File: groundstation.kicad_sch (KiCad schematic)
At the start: 0 parts

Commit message: added display receptacle port for 7in TFT
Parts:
- added C1: C_Small_US, Capacitor_THT:C_Disc_D3.0mm_W1.6mm_P2.50mm, symbol Device:C_Small_US
- added J1: USB_C_Receptacle_USB2.0_16P, Connector_USB:USB_C_Receptacle_G-Switch_GT-USB-7010ASV, symbol Connector:USB_C_Receptacle_USB2.0_16P
- added J2: 62684-402100ALF, CONN_62684-402100ALF_AMP, symbol FCC 40 0.5mm:62684-402100ALF
- added R1, R2: 22, Resistor_SMD:R_0402_1005Metric, symbol Device:R_Small
- added R3, R4: 5.1k, Resistor_SMD:R_0402_1005Metric, symbol Device:R_Small
- added R5: R_Small, Capacitor_THT:C_Disc_D3.0mm_W1.6mm_P2.50mm, symbol Device:R_Small
- added SW1: SW_Push, Resistor_SMD:R_0402_1005Metric, symbol Switch:SW_Push
- added U1: ESP32-S3-WROOM-1, RF_Module:ESP32-S3-WROOM-1, symbol RF_Module:ESP32-S3-WROOM-1
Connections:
- new net: C1.1, R5.1, SW1.2
- new net: J1.B5 (CC2), R4.2
- new net: R1.1, U1.13 (USB_D-)
- new net: R2.1, U1.14 (USB_D+)
- new net: R5.2, U1.3 (EN)
- new net: J1.A6 (D+), J1.B6 (D+), R2.2
- new net: J1.A7 (D-), J1.B7 (D-), R1.2
- new net: J1.A5 (CC1), R3.2
- new net +3V3: U1.2 (3V3)
- new net GND: C1.2, J1.A1 (GND), J1.A12 (GND), J1.B1 (GND), J1.B12 (GND), J1.S1 (SHIELD), R3.1, R4.1, SW1.1, U1.1 (GND), U1.40 (GND), U1.41 (GND)
- new net VBUS: J1.A4 (VBUS), J1.A9 (VBUS), J1.B4 (VBUS), J1.B9 (VBUS)
- no-connect marks 0 -> 6

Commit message: Update schematicand PCB
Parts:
- removed C1: C_Small_US, Capacitor_THT:C_Disc_D3.0mm_W1.6mm_P2.50mm, symbol Device:C_Small_US
- removed J2: 62684-402100ALF, CONN_62684-402100ALF_AMP, symbol FCC 40 0.5mm:62684-402100ALF
- added 2.2uF1, 2.2uF2: C_Small_US, Capacitor_SMD:C_0402_1005Metric, symbol Device:C_Small_US
- added C1: ?, symbol Device:C
- added C10: 1u, symbol Device:C
- added C11: 22u, Capacitor_SMD:C_0603_1608Metric, symbol Device:C
- added C12: 10u, symbol Device:C
- added C2, C3, C4, C5, C6: 1uF, Capacitor_SMD:C_0402_1005Metric, symbol Device:C_Small_US
- added C7: 10u, symbol Device:C_Polarized
- added C8: 0.1u, symbol Device:C
- added C9: 2.2uF, Capacitor_SMD:C_0402_1005Metric, symbol Device:C_Small_US
- added DS1: NHD-C12832A1Z-FSW-FBW-3V3, Ground_Station:LCD_NHD-C12832A1Z-FSW-FBW-3V3, symbol NHD LCD display:NHD-C12832A1Z-FSW-FBW-3V3
- added LED1: LTST-C170KRKT, Ground_Station:LED_LTST-C170KRKT_LTO-M, symbol LTST-C170krkt:LTST-C170KRKT
- added R6: 410, symbol Device:R_Small
- added R7: 10k, Resistor_SMD:R_0402_1005Metric, symbol Device:R_Small
- added U3: AMS1117-3.3, Package_TO_SOT_SMD:SOT-223-3_TabPin2, symbol Regulator_Linear:AMS1117-3.3
- R5: value R_Small -> ?; footprint Capacitor_THT:C_Disc_D3.0mm_W1.6mm_P2.50mm -> Resistor_SMD:R_0402_1005Metric
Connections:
- net +3V3: now also C11.1, C7.1, C8.1, DS1.12 (VDD), DS1.A (LED+), LED1.2, R7.2, U3.2 (VO)
- net GND: now also C1.1, C10.1, C11.2, C12.2, C2.1, C3.1, C4.1, C5.1, C6.1, C7.2, C8.2, C9.1, DS1.11 (VSS), DS1.K (LED-), R6.1, U3.1 (GND)
- net at R5.1, SW1.2: now also C1.2
- net SCL: now reaches U1.15 (IO3)
- net SCL: now also DS1.14 (SCL)
- net CS1: now reaches U1.27 (IO0)
- net CS1: now also DS1.17 (~{CS1})
- net EN: now reaches R5.2, U1.3 (EN)
- net EN: now also C10.2, R7.1
- net A0: now reaches U1.38 (IO2)
- net A0: now also DS1.15 (A0)
- net RST: now reaches U1.39 (IO1)
- net RST: now also DS1.16 (~{RST})
- net SI: now reaches U1.4 (IO4)
- net SI: now also DS1.13 (SI)
- net VBUS renamed 5V
- net 5V: now also C12.1, U3.3 (VI)
- new net: LED1.1, R6.2
- new net: 2.2uF2.2, DS1.6 (C2-)
- new net: 2.2uF2.1, DS1.7 (C2+)
- new net: 2.2uF1.1, DS1.8 (C1+)
- new net: 2.2uF1.2, DS1.9 (C1-)
- new net V0: C2.2, DS1.1 (V0)
- new net V1: C3.2, DS1.2 (V1)
- new net V2: C4.2, DS1.3 (V2)
- new net V3: C5.2, DS1.4 (V3)
- new net V4: C6.2, DS1.5 (V4)
- new net Vout: C9.2, DS1.10 (VOUT)
- no-connect marks 6 -> 31
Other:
- note added: "Power LDO for Vdd"
- note added: "coupling caps for the display"
- moved on the sheet: J1, R1, R2, R3, R4, R5, SW1, U1

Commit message: done with schematic (hopefully)
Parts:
- removed 2.2uF1, 2.2uF2: C_Small_US, Capacitor_SMD:C_0402_1005Metric, symbol Device:C_Small_US
- removed C2, C3, C4, C5, C6: 1uF, Capacitor_SMD:C_0402_1005Metric, symbol Device:C_Small_US
- removed C7: 10u, symbol Device:C_Polarized
- removed C9: 2.2uF, Capacitor_SMD:C_0402_1005Metric, symbol Device:C_Small_US
- removed LED1: LTST-C170KRKT, Ground_Station:LED_LTST-C170KRKT_LTO-M, symbol LTST-C170krkt:LTST-C170KRKT
- added C13, C14: 2.2uF, Capacitor_SMD:C_0402_1005Metric, symbol Device:C
- added C2: 2.2u, Capacitor_SMD:C_0402_1005Metric, symbol Device:C
- added C3, C4, C6, C9: 1u, Capacitor_SMD:C_0402_1005Metric, symbol Device:C
- added C5: 1.0u, Capacitor_SMD:C_0402_1005Metric, symbol Device:C
- added C7: 10uF, Capacitor_SMD:C_0805_2012Metric, symbol Device:C
- added D1: LED, LED_THT:LED_D1.8mm_W1.8mm_H2.4mm_Horizontal_O1.27mm_Z1.6mm, symbol Device:LED
- added J2: Conn_01x02_Pin, Connector_PinHeader_2.54mm:PinHeader_1x02_P2.54mm_Vertical, symbol Connector:Conn_01x02_Pin
- C1: value ? -> 0.1u; footprint (none) -> Capacitor_SMD:C_0402_1005Metric
- C10: footprint (none) -> Capacitor_SMD:C_0402_1005Metric
- C11: footprint Capacitor_SMD:C_0603_1608Metric -> Capacitor_SMD:C_0805_2012Metric
- C12, C8: footprint (none) -> Capacitor_SMD:C_0805_2012Metric
- R5: value ? -> 0
- R6: footprint (none) -> Resistor_SMD:R_0402_1005Metric
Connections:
- net +3V3: now also C7.1, D1.2 (A)
- net GND: now also C2.2, C3.2, C4.2, C5.2, C6.2, C7.2, C9.2, J2.2 (Pin_2)
- net at R6.2: now also D1.1 (K)
- net Display_SI: now reaches U1.5 (IO5)
- net Display_SI: now also DS1.13 (SI)
- net at DS1.6 (C2-): now also C13.2
- net at DS1.7 (C2+): now also C13.1
- net at DS1.8 (C1+): now also C14.1
- net at DS1.9 (C1-): now also C14.2
- net A0 renamed Display_A0
- net Display_A0: now also U1.15 (IO3); no longer U1.38 (IO2)
- net CS1: no longer names the net of U1.27 (IO0)
- net CS1: now also J2.1 (Pin_1); no longer DS1.17 (~{CS1})
- net RST renamed Display_CS1
- net Display_CS1: now also DS1.17 (~{CS1}); no longer DS1.16 (~{RST})
- net SCL renamed Display_SCL
- net Display_SCL: now also U1.4 (IO4); no longer U1.15 (IO3)
- removed net SI: DS1.13 (SI), U1.4 (IO4)
- net V0: no longer names the net of DS1.1 (V0)
- net V0: now also C9.1
- net V1: no longer names the net of DS1.2 (V1)
- net V1: now also C6.1
- net V2: no longer names the net of DS1.3 (V2)
- net V2: now also C5.1
- net V3: no longer names the net of DS1.4 (V3)
- net V3: now also C4.1
- net V4: no longer names the net of DS1.5 (V4)
- net V4: now also C3.1
- net Vout: no longer names the net of DS1.10 (VOUT)
- net Vout: now also C2.1
- new net Display_RST: DS1.16 (~{RST}), U1.38 (IO2)
- no-connect marks 31 -> 30
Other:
- note added: "Charging Pumps for LCD"
- note added: "EN pull up circuit and OFF switch"
- note added: "ESP32-S3 indicator LED"
- note added: "Power LDO for usb 5V to esp32 3V3 VDD"
- note added: "low and high frequency filter"
- note removed: "Power LDO for Vdd"
- note removed: "coupling caps for the display"
- moved on the sheet: C1, C10, C11, C12, DS1, R5, R6, R7, SW1, U3

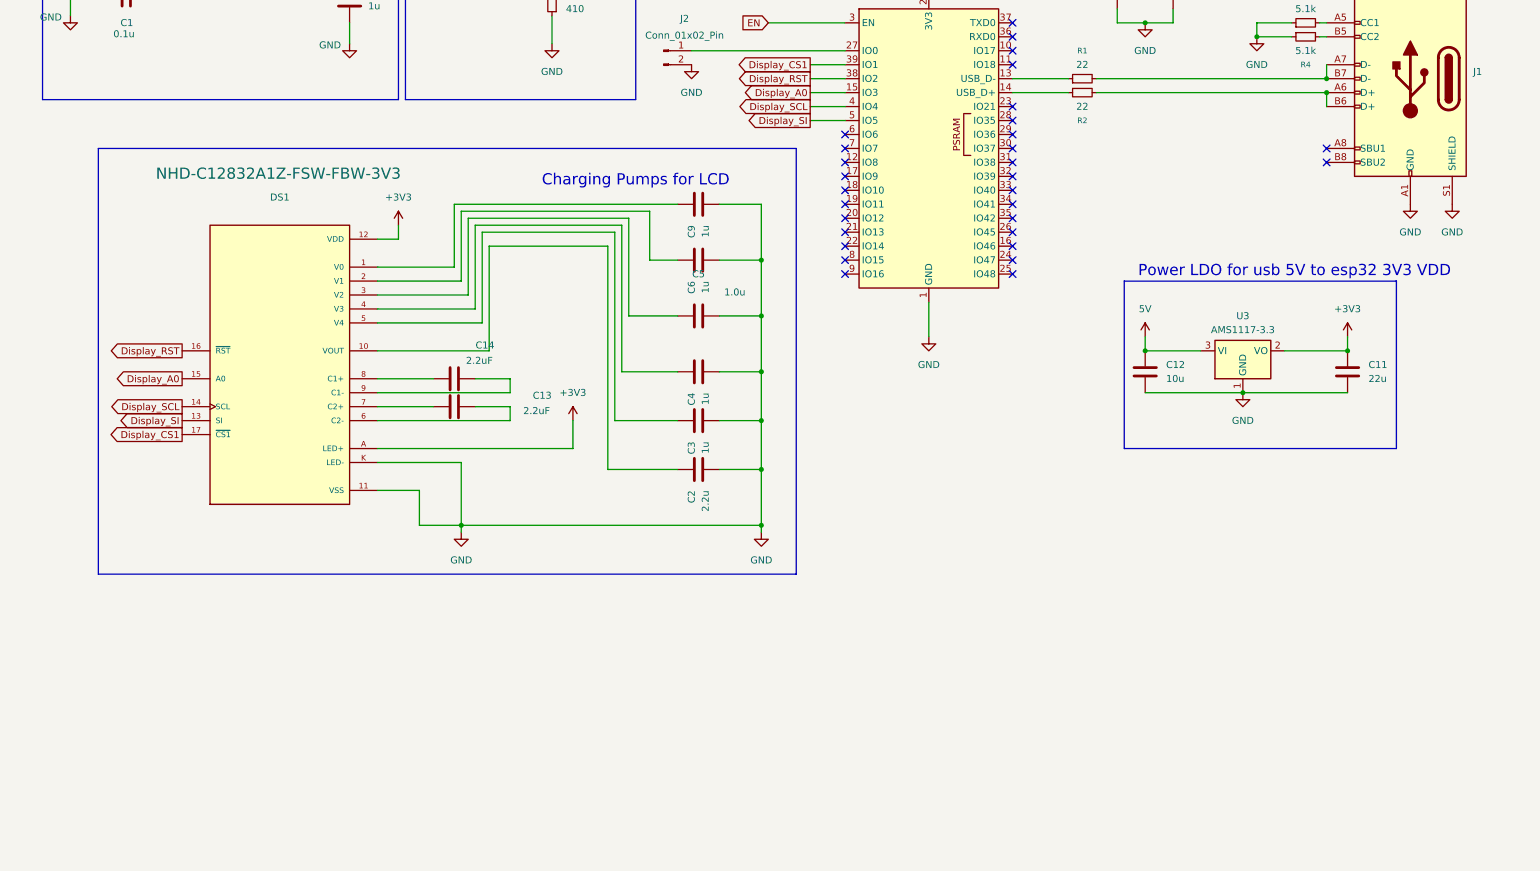
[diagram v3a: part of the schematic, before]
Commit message: added GPS module
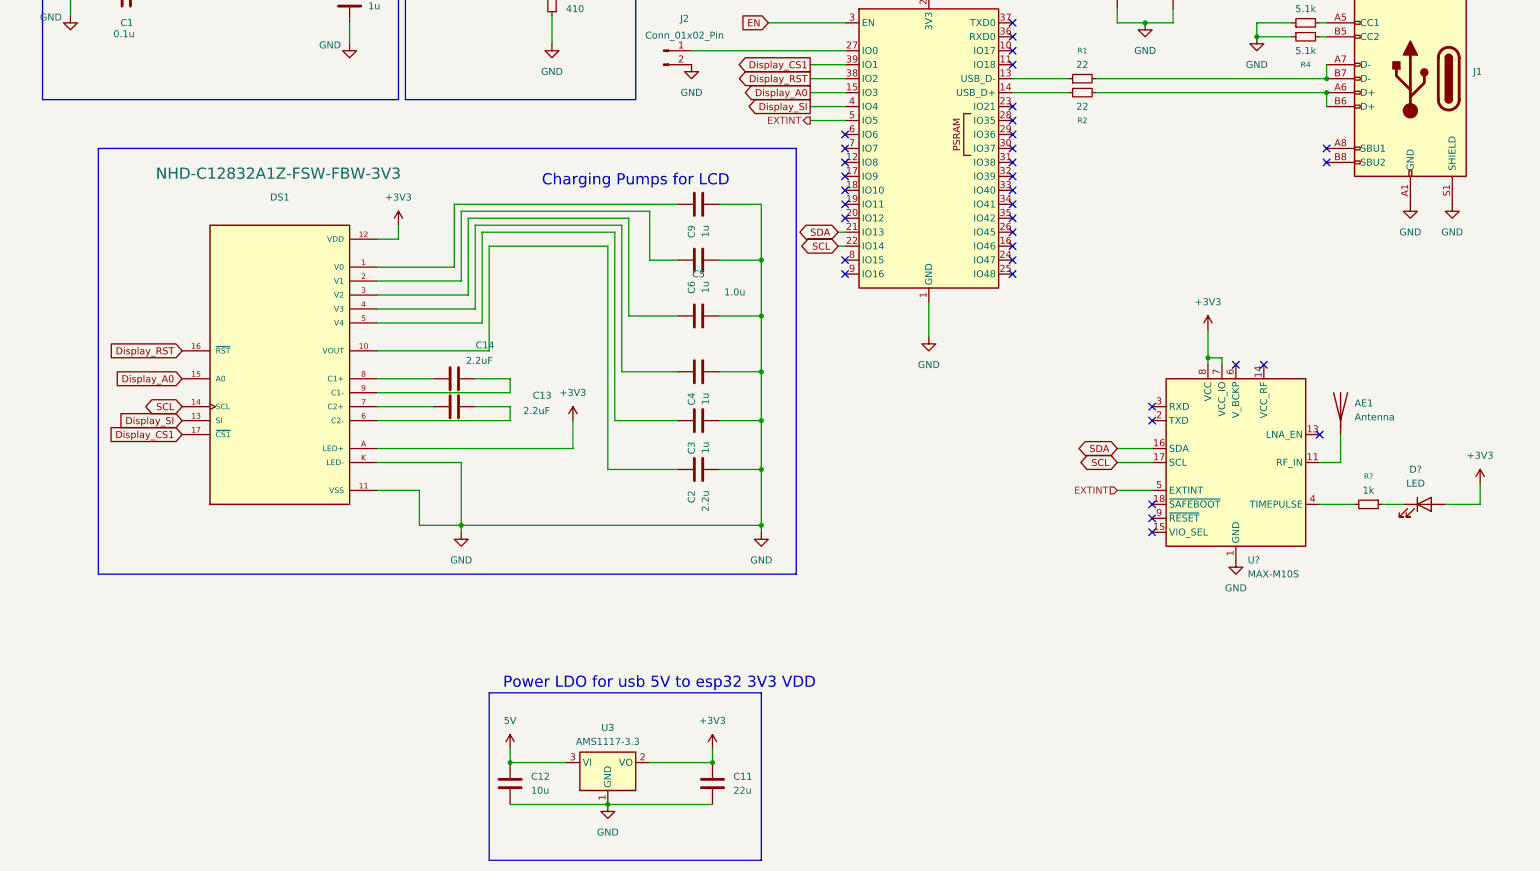
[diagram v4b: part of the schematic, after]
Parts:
- added AE1: Antenna, symbol Device:Antenna
- added D?: LED, LED_SMD:LED_0805_2012Metric, symbol Device:LED
- added R?: 1k, Resistor_SMD:R_0402_1005Metric, symbol Device:R_Small
- added U?: MAX-M10S, RF_GPS:ublox_MAX, symbol RF_GPS:MAX-M10S
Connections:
- net +3V3: now also D?.2 (A), U?.7 (VCC_IO), U?.8 (VCC)
- net Display_SI: now also U1.4 (IO4); no longer U1.5 (IO5)
- net GND: now also U?.1 (GND), U?.10 (GND), U?.12 (GND)
- net SDA: now reaches U1.21 (IO13)
- net SDA: now also U?.16 (SDA)
- net SCL: now reaches U1.22 (IO14)
- net SCL: now also DS1.14 (SCL), U?.17 (SCL)
- removed net Display_SCL: DS1.14 (SCL), U1.4 (IO4)
- new net: AE1.1 (A), U?.11 (RF_IN)
- new net: R?.2, U?.4 (TIMEPULSE)
- new net: D?.1 (K), R?.1
- new net EXTINT: U1.5 (IO5), U?.5 (EXTINT)
- no-connect marks 30 -> 36
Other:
- moved on the sheet: C11, C12, U3

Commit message: dunno, random adds
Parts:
- added C15, C16, C17, C18, C19: C_Small, symbol Device:C_Small
- added FL1: 0900FM15K0039, RF_Converter:Balun_Johanson_0900FM15K0039, symbol Filter:0900FM15K0039
- added J3: Conn_Coaxial, Connector_Coaxial:SMA_Samtec_SMA-J-P-H-ST-EM1_EdgeMount, symbol Connector:Conn_Coaxial
- added L1, L2: L_Small, symbol Device:L_Small
- added U4: SX1262IMLTRT, Package_DFN_QFN:QFN-24-1EP_4x4mm_P0.5mm_EP2.6x2.6mm, symbol RF:SX1262IMLTRT
- added U5: BGS12WN6E6327, Package_LGA:Infineon_PG-TSNP-6-10_0.7x1.1mm_0.7x1.1mm_P0.4mm, symbol RF_Switch:BGS12WN6E6327
- AE1: footprint (none) -> Connector_Coaxial:SMA_BAT_Wireless_BWSMA-KWE-Z001
- gave numbers to parts that had none: 3
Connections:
- net GND: now also C15.2, C16.2, C18.2, C19.2, J3.2 (Ext), U4.2 (GND), U4.20 (GND), U4.25 (GND), U4.5 (GND), U4.8 (GND)
- new net: C15.1, C16.1, L1.2, U4.24 (VR_PA)
- new net: C17.1, C18.1, L2.1
- new net: C19.1, J3.1 (In), L2.2
- new net: FL1.1 (RFO), L1.1, U4.23 (RFO)
- new net: FL1.10 (GND), FL1.2 (GND), FL1.5 (GND), FL1.7 (GND), FL1.9 (GND)
- new net: FL1.3 (RFI_N), U4.22 (RFI_N)
- new net: FL1.4 (RFI_P), U4.21 (RFI_P)
- new net: FL1.6 (SW_RFI), U5.3 (RF1)
- new net: FL1.8 (SW_RFO), U5.1 (RF2)
- new net: C17.2, U5.5 (RFIN)
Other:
- moved on the sheet: AE1, C11, C12, D2, R8, U2, U3
